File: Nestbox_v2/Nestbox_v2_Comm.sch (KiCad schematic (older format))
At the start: 7 parts, among them Q601 Q_PMOS_DGS, U601 XBee-S2C-802.15.4_SMT, U602 RN2483, U603 ESP-12S

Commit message: restructured top level sheet with hierarchical labels, assigned most GPIOs
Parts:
- removed Q601: Q_PMOS_DGS, symbol Q_PMOS_DGS
- removed U601: XBee-S2C-802.15.4_SMT, symbol XBee-S2C-802.15.4_SMT
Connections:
- net labels added: ESP12_ENABLE, ESP12_RX, ESP12_TX
- net labels removed: DATA_Enable_N, DATA_RX, DATA_TX, VCC_XBee
- wire segments 21 -> 15
- no-connect marks 39 -> 10
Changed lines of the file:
@@
 LIBS:SeeedOPL-Transistor-2016
 LIBS:Nestbox_v2-cache
-EELAYER 26 0
+EELAYER 25 0
 EELAYER END
 $Descr A4 11693 8268
@@
 Wire Wire Line
 	9150 4400 9600 4400
-Text GLabel 9600 4400 2    60   Input ~ 0
-LORA_RX
-Text GLabel 9600 4500 2    60   Input ~ 0
-LORA_TX
 $Comp
 L GND #PWR060
@@
 Wire Wire Line
 	6750 3900 7450 3900
-Text GLabel 6750 3900 0    60   Input ~ 0
-LORA_RST_N
 Wire Wire Line
 	6900 3900 6900 3700
@@
 	1    0    0    -1
 $EndComp
-NoConn ~ 5250 1150
-NoConn ~ 5250 1250
-NoConn ~ 5250 1350
-NoConn ~ 5250 1450
-NoConn ~ 5250 1550
-NoConn ~ 5250 1650
-NoConn ~ 5250 1750
-NoConn ~ 5250 1850
-NoConn ~ 5250 1950
-NoConn ~ 5250 2350
-NoConn ~ 5250 2450
-NoConn ~ 5250 2600
-NoConn ~ 5250 2700
-NoConn ~ 5250 2800
-NoConn ~ 5250 2900
-NoConn ~ 5250 3000
-NoConn ~ 5250 3200
-NoConn ~ 3400 2400
-NoConn ~ 3400 2500
-NoConn ~ 3400 2600
-NoConn ~ 3400 2700
-NoConn ~ 3400 2800
-NoConn ~ 3400 2900
-NoConn ~ 3400 3000
-NoConn ~ 3400 3100
-NoConn ~ 3400 3200
-NoConn ~ 3400 2300
-NoConn ~ 3400 2000
-NoConn ~ 3400 1900
-Wire Wire Line
-	3400 1250 3200 1250
-Wire Wire Line
-	3200 1250 3200 1750
-Wire Wire Line
-	3200 1350 3400 1350
-Wire Wire Line
-	3200 1450 3400 1450
-Connection ~ 3200 1350
-Wire Wire Line
-	3200 1550 3400 1550
-Connection ~ 3200 1450
-Wire Wire Line
-	3200 1650 3400 1650
-Connection ~ 3200 1550
-$Comp
-L GND #PWR078
-U 1 1 59FDFCD3
-P 3200 1750
-F 0 "#PWR078" H 3200 1500 50  0001 C CNN
-F 1 "GND" H 3205 1577 50  0000 C CNN
-F 2 "" H 3200 1750 50  0000 C CNN
-F 3 "" H 3200 1750 50  0000 C CNN
-	1    3200 1750
-	1    0    0    -1
-$EndComp
-Connection ~ 3200 1650
-Wire Wire Line
-	3400 1150 2950 1150
-Text Label 2950 1150 0    60   ~ 0
-VCC_XBee
-Text GLabel 5250 2100 2    60   Input ~ 0
-DATA_RX
-Text GLabel 5250 2200 2    60   Input ~ 0
-DATA_TX
-$Comp
-L XBee-S2C-802.15.4_SMT U601
-U 1 1 59FE0508
-P 3950 1050
-F 0 "U601" H 4325 1197 60  0000 C CNN
-F 1 "XBee-S2C-802.15.4_SMT" H 4325 1091 60  0000 C CNN
-F 2 "" H 3950 1050 60  0001 C CNN
-F 3 "" H 3950 1050 60  0001 C CNN
-	1    3950 1050
-	1    0    0    -1
-$EndComp
-$Comp
-L Q_PMOS_DGS Q601
-U 1 1 59FE0AF1
-P 1750 1450
-F 0 "Q601" H 1956 1496 50  0000 L CNN
-F 1 "Q_PMOS_DGS" H 1956 1405 50  0000 L CNN
-F 2 "" H 1950 1550 50  0000 C CNN
-F 3 "" H 1750 1450 50  0000 C CNN
-	1    1750 1450
-	1    0    0    -1
-$EndComp
-$Comp
-L +3.3V #PWR079
-U 1 1 59FE0C6C
-P 1850 1200
-F 0 "#PWR079" H 1850 1050 50  0001 C CNN
-F 1 "+3.3V" H 1865 1373 50  0000 C CNN
-F 2 "" H 1850 1200 50  0000 C CNN
-F 3 "" H 1850 1200 50  0000 C CNN
-	1    1850 1200
-	1    0    0    -1
-$EndComp
-Wire Wire Line
-	1850 1000 1850 1250
-Wire Wire Line
-	1850 1650 1850 2100
-Text Label 1850 2100 1    60   ~ 0
-VCC_XBee
-Text GLabel 1550 1450 0    60   Input ~ 0
-DATA_Enable_N
 $Comp
 L R R601
@@
 	1    0    0    -1
 $EndComp
-Text GLabel 2700 5700 0    60   Input ~ 0
-DATA_Enable_N
 NoConn ~ 2700 5600
 NoConn ~ 2700 5800
@@
 Wire Wire Line
 	3900 6200 3700 6200
-Text GLabel 3700 5500 2    60   Input ~ 0
-DATA_RX
-Text GLabel 3700 5600 2    60   Input ~ 0
-DATA_TX
 Text Notes 1900 6850 0    60   Italic 0
 TODO: break out all necessary pins for flashing the ESP on the PCB. \nInclude a debugger header compatible with standard FTDI boards:\nhttps://www.sparkfun.com/products/9873 for example\n\n
 Text Notes 1900 4850 0    60   ~ 0
 UART0 will output some printed information when the device is \npowered on and is booting up. If this issue exerts influence on some \nspecific applications, users can exchange the inner pins of UART when \ninitializing, that is to say, exchange U0TXD, U0RXD with U0RTS, \nU0CTS (IO15 & IO13)\n.
+Text HLabel 3800 5500 2    60   Input ~ 0
+ESP12_TX
+Wire Wire Line
+	3800 5500 3700 5500
+Text HLabel 3800 5600 2    60   Input ~ 0
+ESP12_RX
+Wire Wire Line
+	3800 5600 3700 5600
+Text HLabel 2550 5700 0    60   Input ~ 0
+ESP12_ENABLE
+Wire Wire Line
+	2550 5700 2700 5700
+Text HLabel 9600 4400 2    60   Input ~ 0
+LORA_RX
+Text HLabel 9600 4500 2    60   Input ~ 0
+LORA_TX
+Text HLabel 6750 3900 0    60   Input ~ 0
+LORA_RST_N
 $EndSCHEMATC

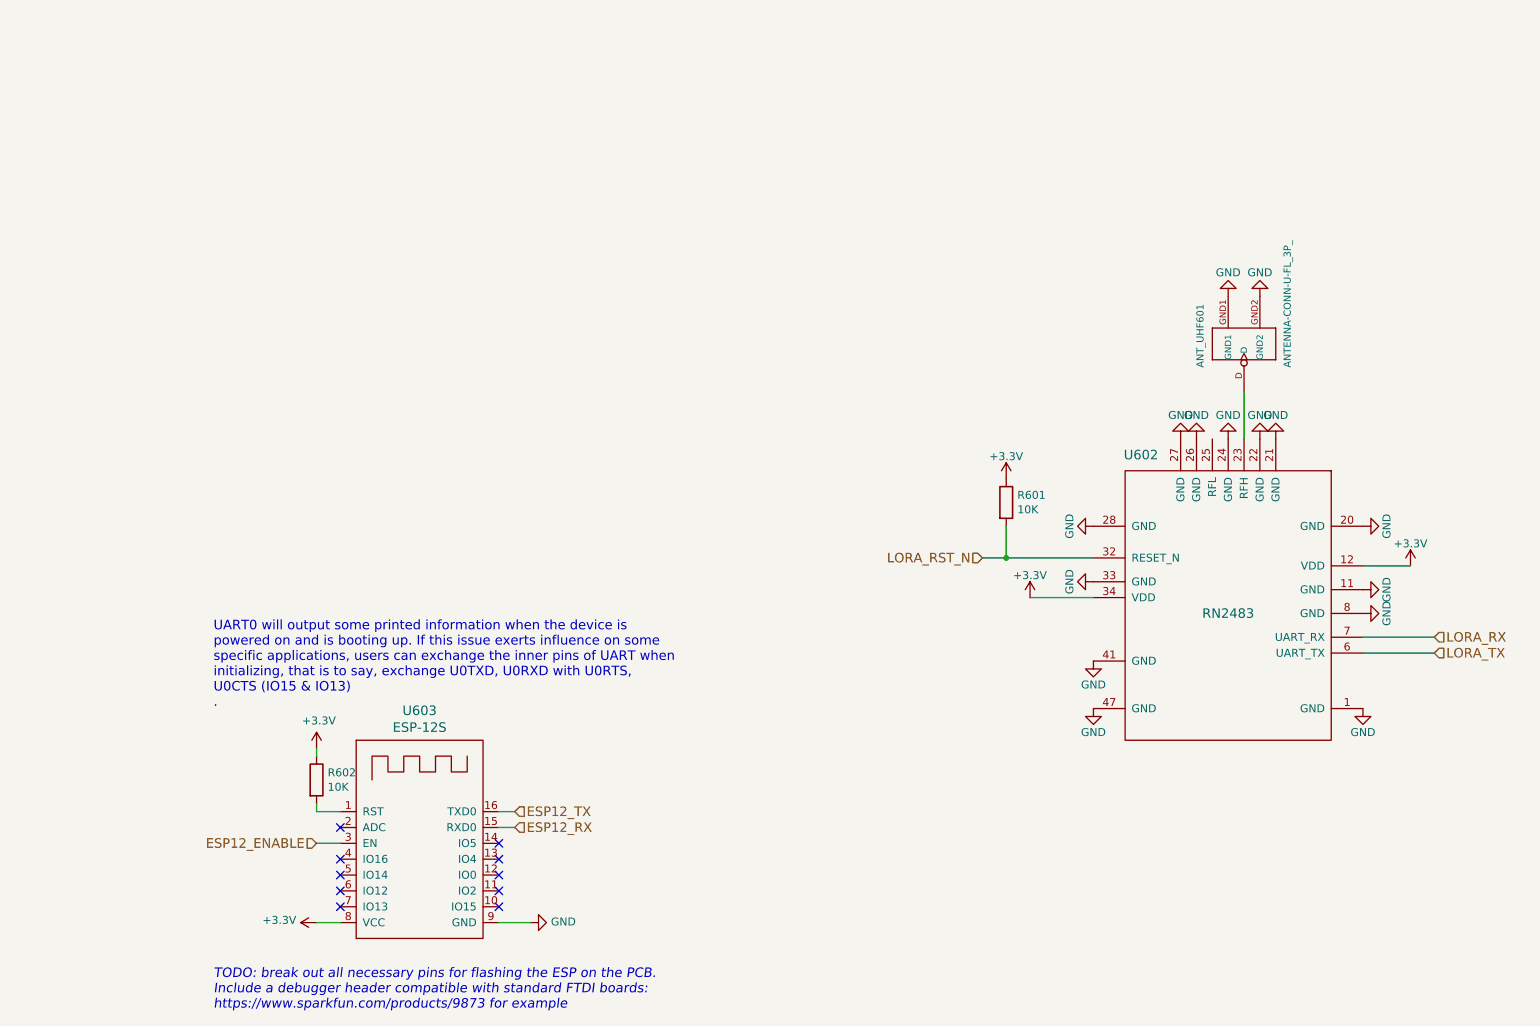
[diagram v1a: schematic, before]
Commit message: added PIR and lightbarrier headers
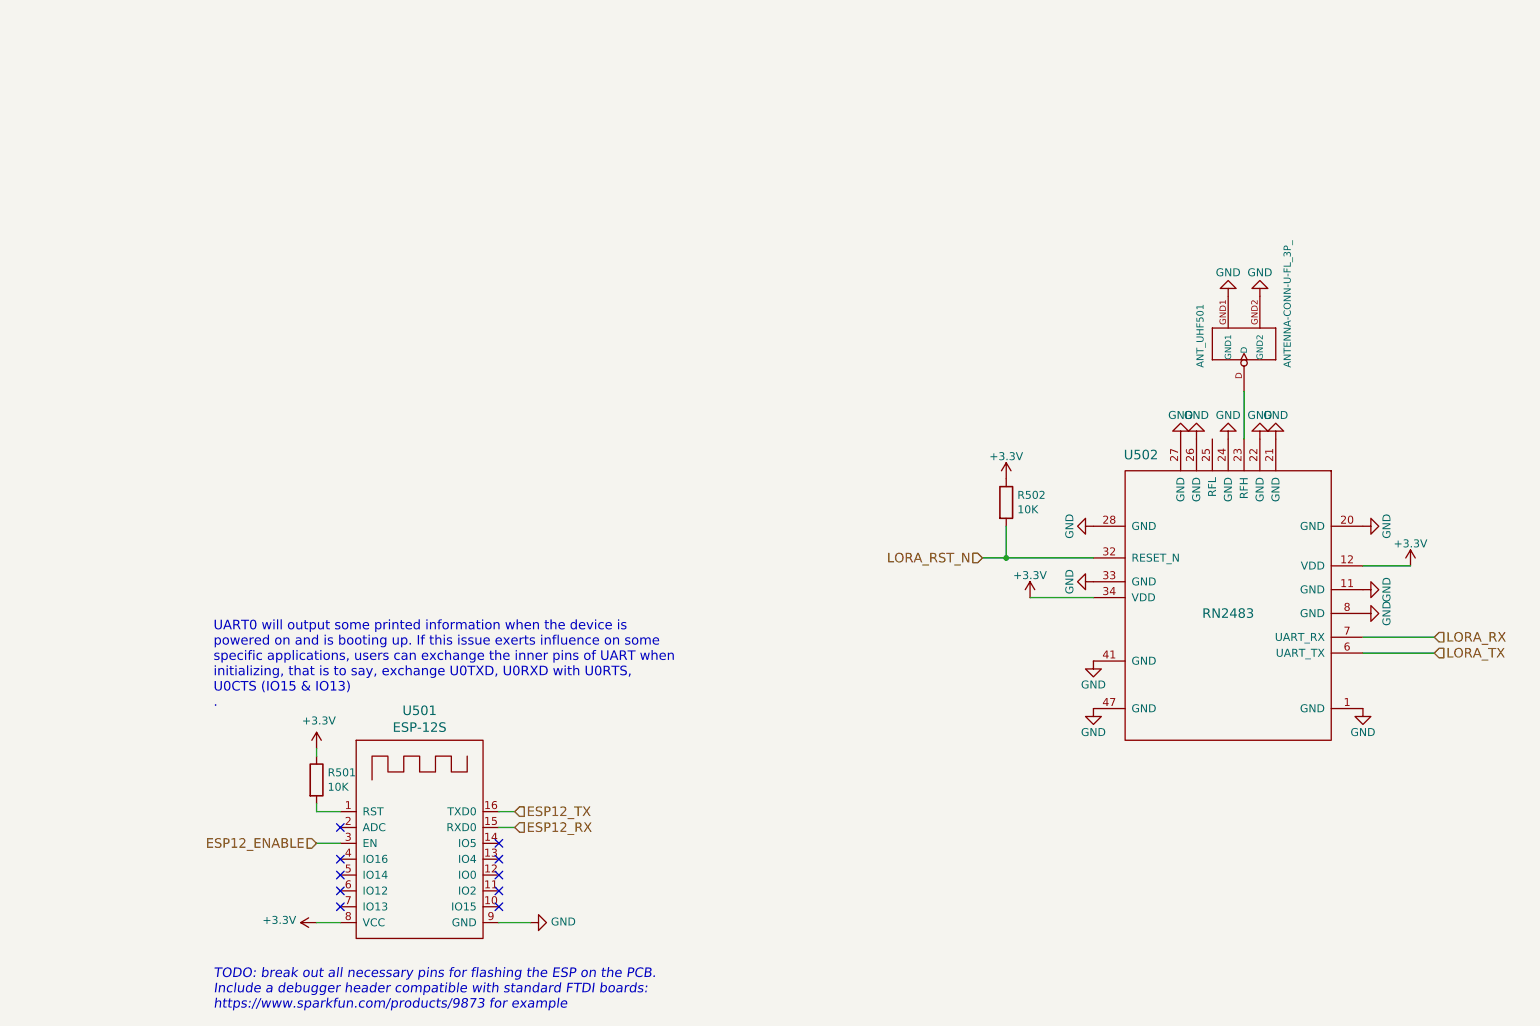
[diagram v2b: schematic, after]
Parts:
- renumbered ANT_UHF601 to ANT_UHF501, R602 to R501, R601 to R502, U603 to U501, U602 to U502
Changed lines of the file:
@@
 $Descr A4 11693 8268
 encoding utf-8
-Sheet 6 7
+Sheet 5 7
 Title ""
 Date ""
@@
 $EndDescr
 $Comp
-L RN2483 U602
+L RN2483 U502
 U 1 1 59F64206
 P 8300 4200
-F 0 "U602" H 7750 5150 60  0000 C CNN
+F 0 "U502" H 7750 5150 60  0000 C CNN
 F 1 "RN2483" H 8300 4150 60  0000 C CNN
 F 2 "Octanis3:RN2483" H 8300 4150 60  0001 C CNN
@@
 	9150 4400 9600 4400
 $Comp
-L GND #PWR060
+L GND #PWR044
 U 1 1 59F64207
 P 9150 4850
-F 0 "#PWR060" H 9150 4600 50  0001 C CNN
+F 0 "#PWR044" H 9150 4600 50  0001 C CNN
 F 1 "GND" H 9150 4700 50  0000 C CNN
 F 2 "" H 9150 4850 50  0000 C CNN
@@
 $EndComp
 $Comp
-L GND #PWR061
+L GND #PWR045
 U 1 1 59F64208
 P 7450 4850
-F 0 "#PWR061" H 7450 4600 50  0001 C CNN
+F 0 "#PWR045" H 7450 4600 50  0001 C CNN
 F 1 "GND" H 7450 4700 50  0000 C CNN
 F 2 "" H 7450 4850 50  0000 C CNN
@@
 $EndComp
 $Comp
-L GND #PWR062
+L GND #PWR046
 U 1 1 59F64209
 P 7450 4550
-F 0 "#PWR062" H 7450 4300 50  0001 C CNN
+F 0 "#PWR046" H 7450 4300 50  0001 C CNN
 F 1 "GND" H 7450 4400 50  0000 C CNN
 F 2 "" H 7450 4550 50  0000 C CNN
@@
 $EndComp
 $Comp
-L GND #PWR063
+L GND #PWR047
 U 1 1 59F6420A
 P 7450 4050
-F 0 "#PWR063" H 7450 3800 50  0001 C CNN
+F 0 "#PWR047" H 7450 3800 50  0001 C CNN
 F 1 "GND" H 7450 3900 50  0000 C CNN
 F 2 "" H 7450 4050 50  0000 C CNN
@@
 $EndComp
 $Comp
-L GND #PWR064
+L GND #PWR048
 U 1 1 59F6420B
 P 7450 3700
-F 0 "#PWR064" H 7450 3450 50  0001 C CNN
+F 0 "#PWR048" H 7450 3450 50  0001 C CNN
 F 1 "GND" H 7450 3550 50  0000 C CNN
 F 2 "" H 7450 3700 50  0000 C CNN
@@
 $EndComp
 $Comp
-L GND #PWR065
+L GND #PWR049
 U 1 1 59F6420C
 P 9150 3700
-F 0 "#PWR065" H 9150 3450 50  0001 C CNN
+F 0 "#PWR049" H 9150 3450 50  0001 C CNN
 F 1 "GND" H 9150 3550 50  0000 C CNN
 F 2 "" H 9150 3700 50  0000 C CNN
@@
 $EndComp
 $Comp
-L GND #PWR066
+L GND #PWR050
 U 1 1 59F6420D
 P 9150 4100
-F 0 "#PWR066" H 9150 3850 50  0001 C CNN
+F 0 "#PWR050" H 9150 3850 50  0001 C CNN
 F 1 "GND" H 9150 3950 50  0000 C CNN
 F 2 "" H 9150 4100 50  0000 C CNN
@@
 $EndComp
 $Comp
-L GND #PWR067
+L GND #PWR051
 U 1 1 59F6420E
 P 9150 4250
-F 0 "#PWR067" H 9150 4000 50  0001 C CNN
+F 0 "#PWR051" H 9150 4000 50  0001 C CNN
 F 1 "GND" H 9150 4100 50  0000 C CNN
 F 2 "" H 9150 4250 50  0000 C CNN
@@
 $EndComp
 $Comp
-L GND #PWR068
+L GND #PWR052
 U 1 1 59F6420F
 P 8600 3150
-F 0 "#PWR068" H 8600 2900 50  0001 C CNN
+F 0 "#PWR052" H 8600 2900 50  0001 C CNN
 F 1 "GND" H 8600 3000 50  0000 C CNN
 F 2 "" H 8600 3150 50  0000 C CNN
@@
 $EndComp
 $Comp
-L GND #PWR069
+L GND #PWR053
 U 1 1 59F64210
 P 8500 3150
-F 0 "#PWR069" H 8500 2900 50  0001 C CNN
+F 0 "#PWR053" H 8500 2900 50  0001 C CNN
 F 1 "GND" H 8500 3000 50  0000 C CNN
 F 2 "" H 8500 3150 50  0000 C CNN
@@
 $EndComp
 $Comp
-L GND #PWR070
+L GND #PWR054
 U 1 1 59F64211
 P 8300 3150
-F 0 "#PWR070" H 8300 2900 50  0001 C CNN
+F 0 "#PWR054" H 8300 2900 50  0001 C CNN
 F 1 "GND" H 8300 3000 50  0000 C CNN
 F 2 "" H 8300 3150 50  0000 C CNN
@@
 $EndComp
 $Comp
-L GND #PWR071
+L GND #PWR055
 U 1 1 59F64212
 P 8100 3150
-F 0 "#PWR071" H 8100 2900 50  0001 C CNN
+F 0 "#PWR055" H 8100 2900 50  0001 C CNN
 F 1 "GND" H 8100 3000 50  0000 C CNN
 F 2 "" H 8100 3150 50  0000 C CNN
@@
 $EndComp
 $Comp
-L GND #PWR072
+L GND #PWR056
 U 1 1 59F64213
 P 8000 3150
-F 0 "#PWR072" H 8000 2900 50  0001 C CNN
+F 0 "#PWR056" H 8000 2900 50  0001 C CNN
 F 1 "GND" H 8000 3000 50  0000 C CNN
 F 2 "" H 8000 3150 50  0000 C CNN
@@
 Connection ~ 6900 3900
 $Comp
-L ANTENNA-CONN-U-FL_3P_ ANT_UHF601
+L ANTENNA-CONN-U-FL_3P_ ANT_UHF501
 U 1 1 59F64215
 P 8400 2550
-F 0 "ANT_UHF601" H 8250 2800 45  0000 L BNN
+F 0 "ANT_UHF501" H 8250 2800 45  0000 L BNN
 F 1 "ANTENNA-CONN-U-FL_3P_" H 8250 2250 45  0000 L BNN
 F 2 "SeeedOPL-Connector-2016:U-FL3P-SMD-2.6X2.6X1.0MM" H 8400 2550 60  0001 C CNN
@@
 	8400 2850 8400 3150
 $Comp
-L GND #PWR073
+L GND #PWR057
 U 1 1 59F64216
 P 8300 2250
-F 0 "#PWR073" H 8300 2000 50  0001 C CNN
+F 0 "#PWR057" H 8300 2000 50  0001 C CNN
 F 1 "GND" H 8300 2100 50  0000 C CNN
 F 2 "" H 8300 2250 50  0000 C CNN
@@
 $EndComp
 $Comp
-L GND #PWR074
+L GND #PWR058
 U 1 1 59F64217
 P 8500 2250
-F 0 "#PWR074" H 8500 2000 50  0001 C CNN
+F 0 "#PWR058" H 8500 2000 50  0001 C CNN
 F 1 "GND" H 8500 2100 50  0000 C CNN
 F 2 "" H 8500 2250 50  0000 C CNN
@@
 	9450 3950 9150 3950
 $Comp
-L +3.3V #PWR075
+L +3.3V #PWR059
 U 1 1 59F64218
 P 6900 3400
-F 0 "#PWR075" H 6900 3250 50  0001 C CNN
+F 0 "#PWR059" H 6900 3250 50  0001 C CNN
 F 1 "+3.3V" H 6900 3540 50  0000 C CNN
 F 2 "" H 6900 3400 50  0000 C CNN
@@
 $EndComp
 $Comp
-L +3.3V #PWR076
+L +3.3V #PWR060
 U 1 1 59F64219
 P 7050 4150
-F 0 "#PWR076" H 7050 4000 50  0001 C CNN
+F 0 "#PWR060" H 7050 4000 50  0001 C CNN
 F 1 "+3.3V" H 7050 4290 50  0000 C CNN
 F 2 "" H 7050 4150 50  0000 C CNN
@@
 $EndComp
 $Comp
-L +3.3V #PWR077
+L +3.3V #PWR061
 U 1 1 59F6421A
 P 9450 3950
-F 0 "#PWR077" H 9450 3800 50  0001 C CNN
+F 0 "#PWR061" H 9450 3800 50  0001 C CNN
 F 1 "+3.3V" H 9450 4090 50  0000 C CNN
 F 2 "" H 9450 3950 50  0000 C CNN
@@
 $EndComp
 $Comp
-L R R601
+L R R502
 U 1 1 59FF56E8
 P 6900 3550
-F 0 "R601" H 6970 3596 50  0000 L CNN
+F 0 "R502" H 6970 3596 50  0000 L CNN
 F 1 "10K" H 6970 3505 50  0000 L CNN
 F 2 "" V 6830 3550 50  0000 C CNN
@@
 $EndComp
 $Comp
-L ESP-12S U603
+L ESP-12S U501
 U 1 1 59FF5CBB
 P 2800 5050
-F 0 "U603" H 3200 5237 60  0000 C CNN
+F 0 "U501" H 3200 5237 60  0000 C CNN
 F 1 "ESP-12S" H 3200 5131 60  0000 C CNN
 F 2 "" H 2800 5050 60  0001 C CNN
@@
 NoConn ~ 3700 5700
 $Comp
-L R R602
+L R R501
 U 1 1 59FF5E36
 P 2550 5300
-F 0 "R602" H 2620 5346 50  0000 L CNN
+F 0 "R501" H 2620 5346 50  0000 L CNN
 F 1 "10K" H 2620 5255 50  0000 L CNN
 F 2 "" V 2480 5300 50  0000 C CNN
@@
 $EndComp
 $Comp
-L +3.3V #PWR080
+L +3.3V #PWR062
 U 1 1 59FF5EE6
 P 2550 5100
-F 0 "#PWR080" H 2550 4950 50  0001 C CNN
+F 0 "#PWR062" H 2550 4950 50  0001 C CNN
 F 1 "+3.3V" H 2565 5273 50  0000 C CNN
 F 2 "" H 2550 5100 50  0000 C CNN
@@
 	2550 5500 2700 5500
 $Comp
-L +3.3V #PWR081
+L +3.3V #PWR063
 U 1 1 59FF5FCD
 P 2550 6200
-F 0 "#PWR081" H 2550 6050 50  0001 C CNN
+F 0 "#PWR063" H 2550 6050 50  0001 C CNN
 F 1 "+3.3V" V 2565 6328 50  0000 L CNN
 F 2 "" H 2550 6200 50  0000 C CNN
@@
 	2550 6200 2700 6200
 $Comp
-L GND #PWR082
+L GND #PWR064
 U 1 1 59FF60B0
 P 3900 6200
-F 0 "#PWR082" H 3900 5950 50  0001 C CNN
+F 0 "#PWR064" H 3900 5950 50  0001 C CNN
 F 1 "GND" V 3905 6072 50  0000 R CNN
 F 2 "" H 3900 6200 50  0000 C CNN
